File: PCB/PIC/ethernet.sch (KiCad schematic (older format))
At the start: 49 parts, among them P1 HR911105A, U1 LAN_8740, U2 SI502

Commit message: CIAA PIC footprints done
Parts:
- removed P1: HR911105A, symbol CONN_14
- added J5: RJ45-TRANSFO, symbol RJ45-TRANSFO
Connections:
- no-connect marks 5 -> 4
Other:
- note removed: "Verificar disponibilidad del conector Ethernet.\nAlternativa: Pulse J0011D01BNL."
- moved on the sheet: C1, C10, C11, C12, C13, C14, C15, C2, C3, C4, C5, C6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

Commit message: Correcciones al esquematico segun rev01
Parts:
- C1, C5, C9: symbol CP1 -> CP1-RESCUE-ciaa-pic
- C10, C11, C12, C13, C14, C15, C2, C3, C4, C6, C63, C7, C8: symbol C -> C-RESCUE-ciaa-pic
- J5: footprint (none) -> footprints:RJ45_TRANSFO
- R1, R10, R11, R113, R12, R13, R139, R14, R140, R15, R16, R17, R18, R19, R2, R20, R21, R3, R31, R4, R5, R6, R7, R8, R81, R9, R91, R92, R95: symbol R -> R-RESCUE-ciaa-pic
- U1: footprint ~ -> footprints:QFN32_Opendous
- U2: footprint ~ -> footprints:4SMD; symbol SI50X -> Si50X
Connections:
- net labels added: +Filter, CRS_DV, MDC, MDIO, RXCLK, RXD0, RXD1, RXD2, RXD3, RXER, RXN, RXP, TXD0, TXD1, TXEN, TXN, TXP, XTAL1, nRST
- wire segments 144 -> 153
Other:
- note added: "Señales TXP,TXN RXP,RXN \n100 ohm par diferencial\n"
- moved on the sheet: C1, C10, C11, C12, C13, C14, C15, C2, C3, C4, C5, C6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

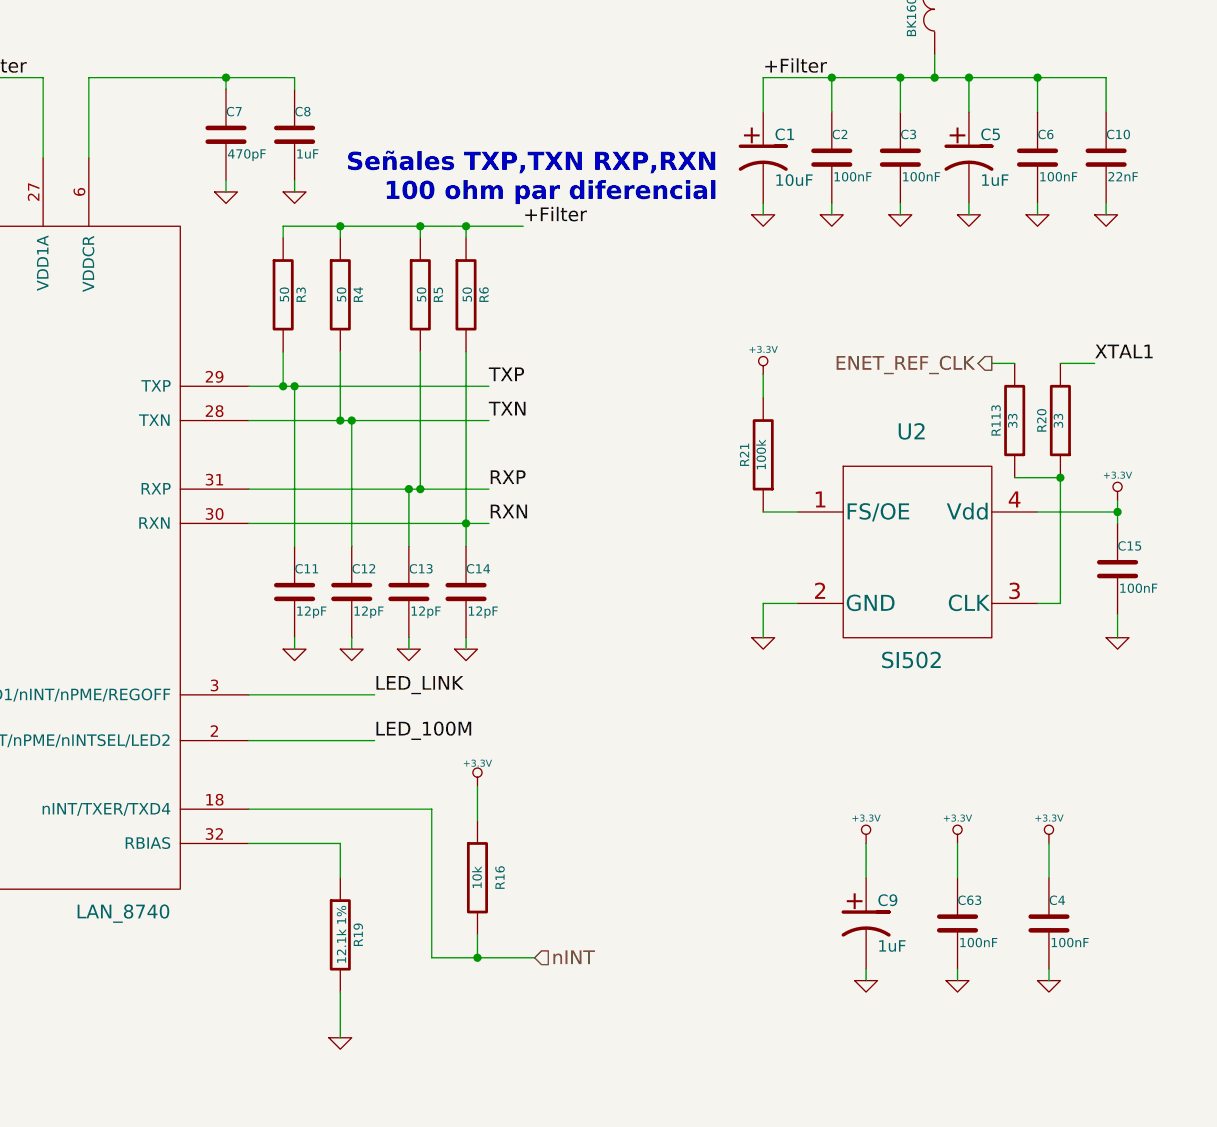
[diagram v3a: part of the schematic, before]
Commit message: elimino conector salida reles
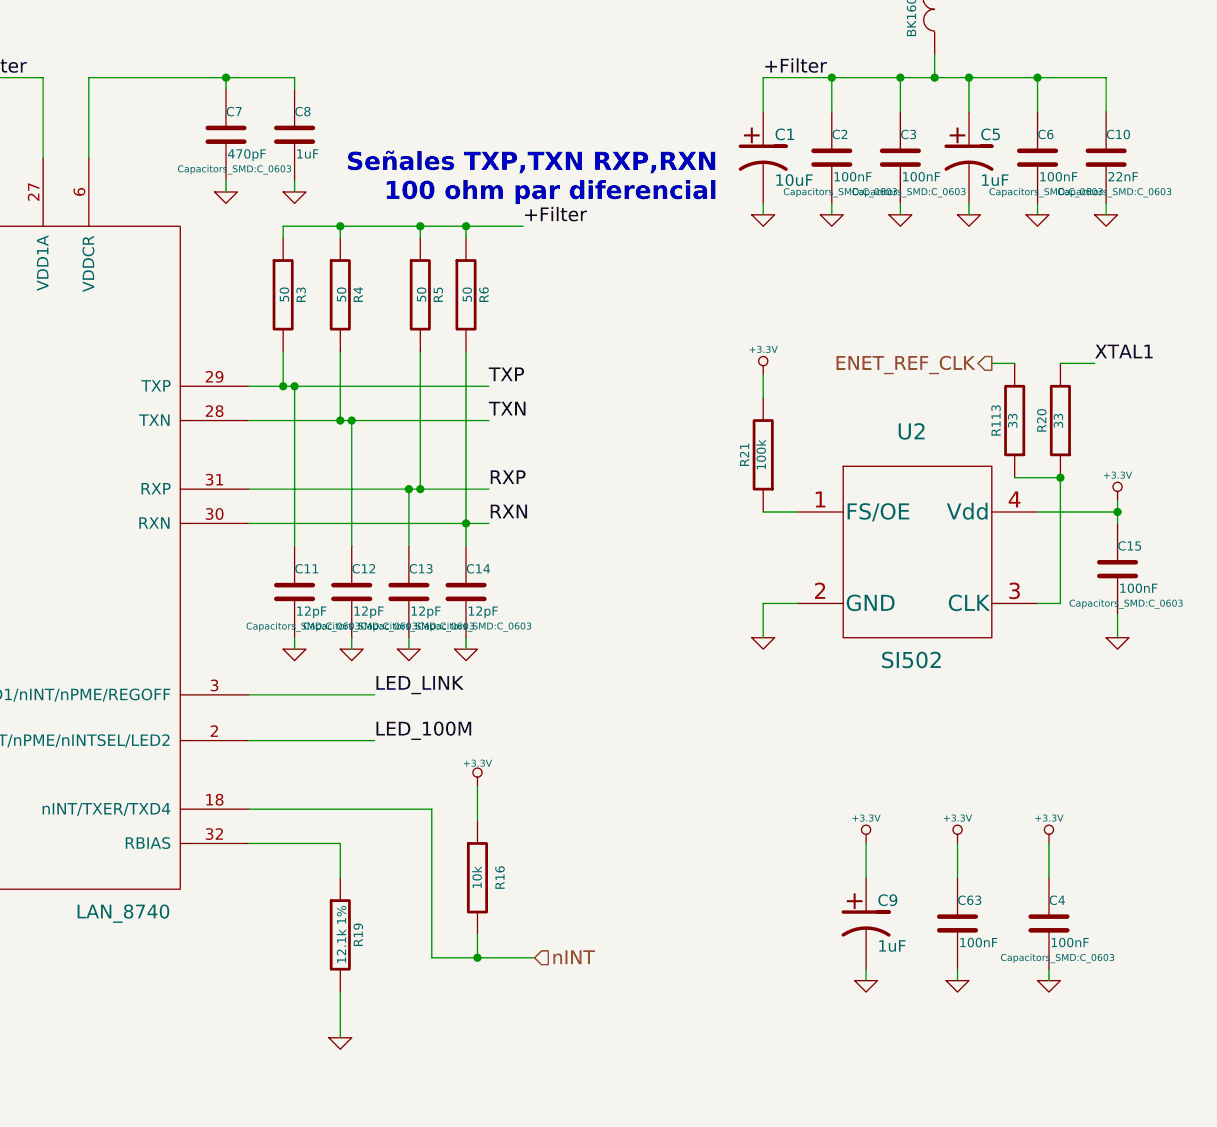
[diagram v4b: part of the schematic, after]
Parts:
- C1, C5, C8, C9, L1: footprint ~ -> (none)
- C10, C11, C12, C13, C14, C15, C2, C3, C4, C6, C63, C7: footprint ~ -> Capacitors_SMD:C_0603
- R1, R10, R11, R113, R12, R13, R139, R14, R140, R15, R16, R17, R18, R19, R2, R20, R21, R3, R31, R4, R5, R6, R7, R8, R81, R9, R91, R92, R95: footprint ~ -> Resistors_SMD:R_0603

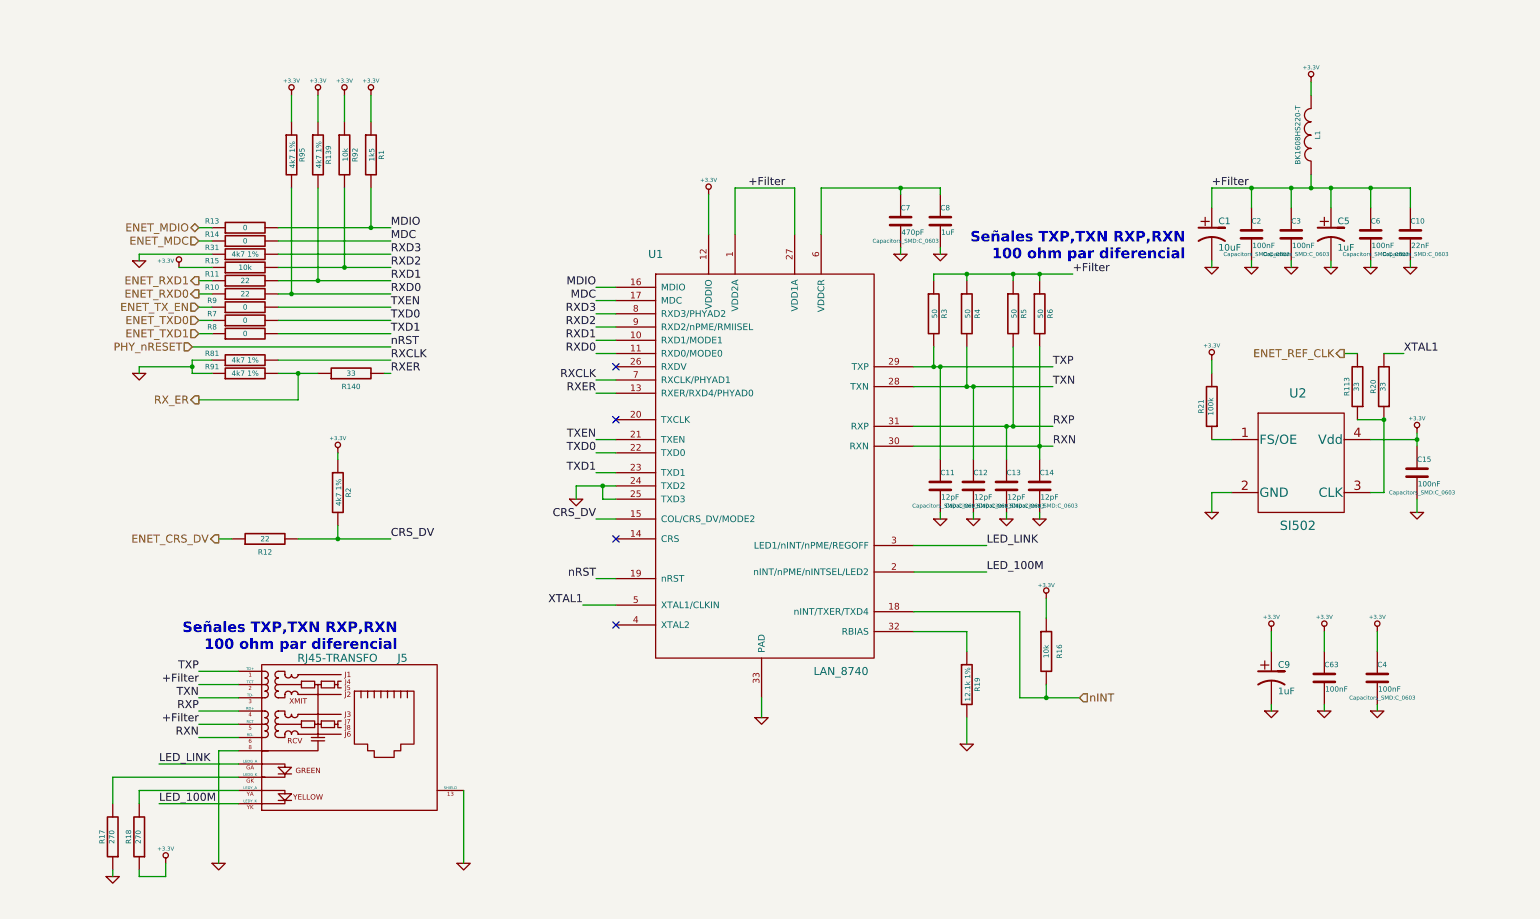
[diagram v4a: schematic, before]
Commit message: rev02 se completa campo num. de frabicante(#manf) CIAA-PIC
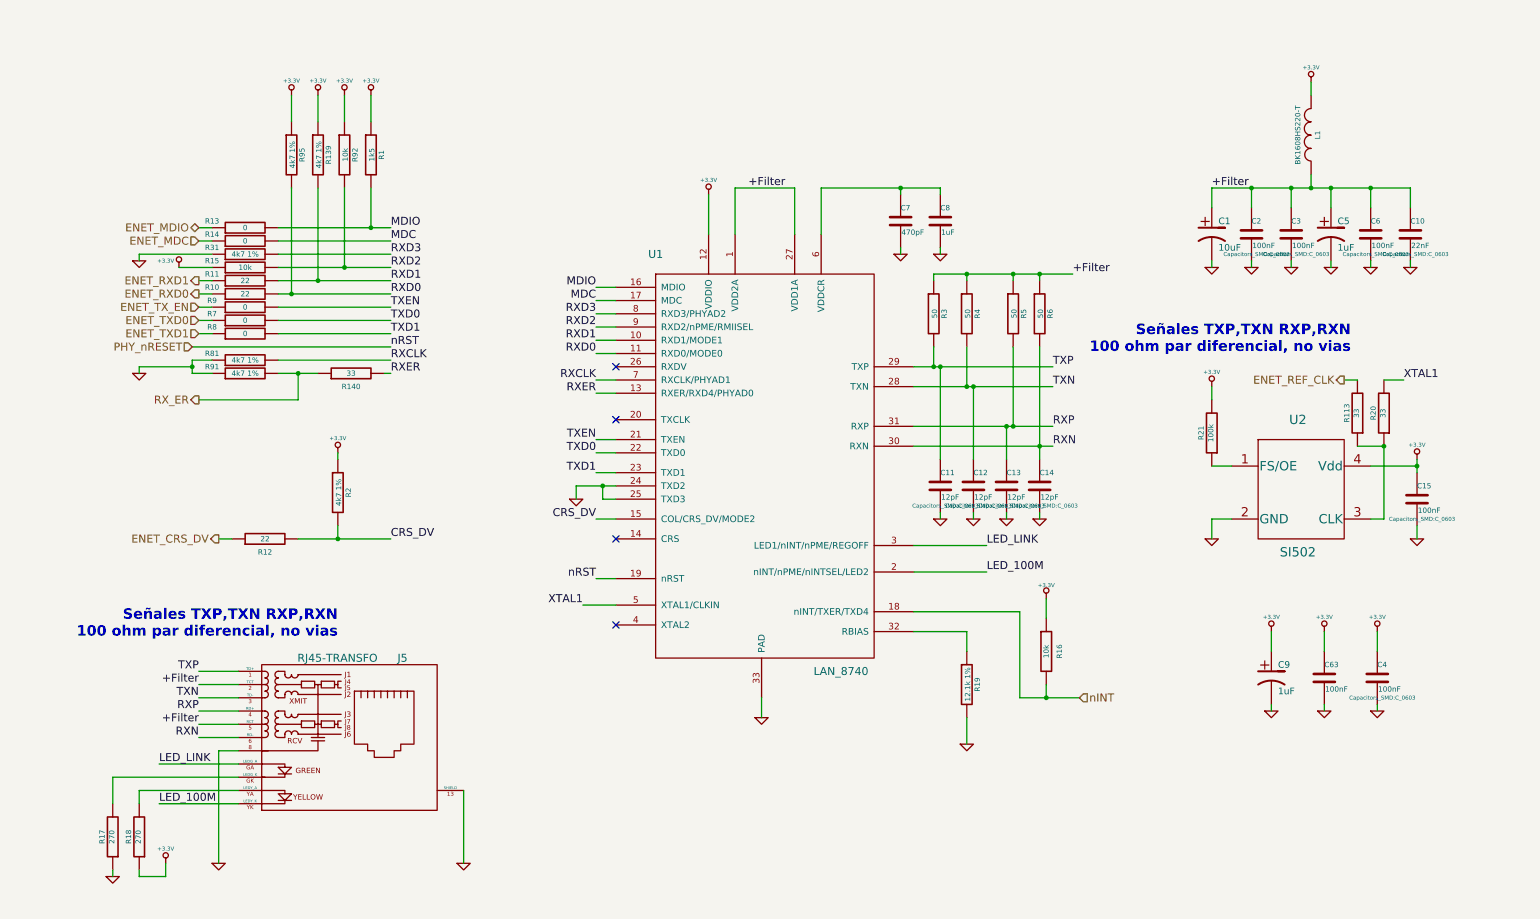
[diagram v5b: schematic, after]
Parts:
- R3, R4, R5, R6: #manf (none) -> RC0603FR-0749R9L
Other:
- note added: "Señales TXP,TXN RXP,RXN \n100 ohm par diferencial, no vias\n"
- note removed: "Señales TXP,TXN RXP,RXN \n100 ohm par diferencial\n"
- moved on the sheet: C15, R113, R20, R21, U2
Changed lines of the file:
@@
 F 0 "C7" H 6800 2250 40  0000 L CNN
 F 1 "470pF" H 6806 2065 40  0000 L CNN
-F 2 "Capacitors_SMD:C_0603" H 6838 2000 30  0000 C CNN
+F 2 "Capacitors_SMD:C_0603" H 6838 2000 30  0001 C CNN
 F 3 "~" H 6800 2150 60  0000 C CNN
 	1    6800 2150
@@
 F 2 "Resistors_SMD:R_0603" V 6980 2850 30  0001 C CNN
 F 3 "~" H 7050 2850 30  0000 C CNN
+F 4 "RC0603FR-0749R9L" V 7050 2850 60  0001 C CNN "#manf"
 	1    7050 2850
 	1    0    0    -1
@@
 F 2 "Resistors_SMD:R_0603" V 7230 2850 30  0001 C CNN
 F 3 "~" H 7300 2850 30  0000 C CNN
+F 4 "RC0603FR-0749R9L" V 7300 2850 60  0001 C CNN "#manf"
 	1    7300 2850
 	1    0    0    -1
@@
 F 2 "Resistors_SMD:R_0603" V 7580 2850 30  0001 C CNN
 F 3 "~" H 7650 2850 30  0000 C CNN
+F 4 "RC0603FR-0749R9L" V 7650 2850 60  0001 C CNN "#manf"
 	1    7650 2850
 	1    0    0    -1
@@
 F 2 "Resistors_SMD:R_0603" V 7780 2850 30  0001 C CNN
 F 3 "~" H 7850 2850 30  0000 C CNN
+F 4 "RC0603FR-0749R9L" V 7850 2850 60  0001 C CNN "#manf"
 	1    7850 2850
 	1    0    0    -1
@@
 L C-RESCUE-ciaa-pic C15
 U 1 1 529F82E9
-P 10700 4050
-F 0 "C15" H 10700 4150 40  0000 L CNN
-F 1 "100nF" H 10706 3965 40  0000 L CNN
-F 2 "Capacitors_SMD:C_0603" H 10738 3900 30  0000 C CNN
-F 3 "~" H 10700 4050 60  0000 C CNN
-	1    10700 4050
+P 10700 4250
+F 0 "C15" H 10700 4350 40  0000 L CNN
+F 1 "100nF" H 10706 4165 40  0000 L CNN
+F 2 "Capacitors_SMD:C_0603" H 10738 4100 30  0000 C CNN
+F 3 "~" H 10700 4250 60  0000 C CNN
+	1    10700 4250
 	1    0    0    -1
 $EndComp
@@
 L Si50X U2
 U 1 1 52BC24C2
-P 9800 4000
-F 0 "U2" H 9800 4550 70  0000 C CNN
-F 1 "SI502" H 9800 3550 70  0000 C CNN
-F 2 "footprints:4SMD" H 9850 3450 60  0001 C CNN
-F 3 "http://www.digikey.com/product-detail/en/silicon-labs/502AAA-ADAG/502AAA-ADAG-ND/4173092" H 8750 7300 60  0001 C CNN
-	1    9800 4000
+P 9800 4200
+F 0 "U2" H 9800 4750 70  0000 C CNN
+F 1 "SI502" H 9800 3750 70  0000 C CNN
+F 2 "footprints:4SMD" H 9850 3650 60  0001 C CNN
+F 3 "http://www.digikey.com/product-detail/en/silicon-labs/502AAA-ADAG/502AAA-ADAG-ND/4173092" H 8750 7500 60  0001 C CNN
+	1    9800 4200
 	1    0    0    -1
 $EndComp
@@
 L +3.3V-RESCUE-ciaa-pic #PWR018
 U 1 1 52BC26E1
-P 10700 3750
-F 0 "#PWR018" H 10700 3710 30  0001 C CNN
-F 1 "+3.3V" H 10700 3860 30  0000 C CNN
-F 2 "" H 10700 3750 60  0000 C CNN
-F 3 "" H 10700 3750 60  0000 C CNN
-	1    10700 3750
+P 10700 3950
+F 0 "#PWR018" H 10700 3910 30  0001 C CNN
+F 1 "+3.3V" H 10700 4060 30  0000 C CNN
+F 2 "" H 10700 3950 60  0000 C CNN
+F 3 "" H 10700 3950 60  0000 C CNN
+	1    10700 3950
 	1    0    0    -1
 $EndComp
@@
 L GND-RESCUE-ciaa-pic #PWR019
 U 1 1 52BC278C
-P 9150 4350
-F 0 "#PWR019" H 9150 4350 30  0001 C CNN
-F 1 "GND" H 9150 4280 30  0001 C CNN
-F 2 "" H 9150 4350 60  0000 C CNN
-F 3 "" H 9150 4350 60  0000 C CNN
-	1    9150 4350
+P 9150 4550
+F 0 "#PWR019" H 9150 4550 30  0001 C CNN
+F 1 "GND" H 9150 4480 30  0001 C CNN
+F 2 "" H 9150 4550 60  0000 C CNN
+F 3 "" H 9150 4550 60  0000 C CNN
+	1    9150 4550
 	1    0    0    -1
 $EndComp
@@
 L R-RESCUE-ciaa-pic R20
 U 1 1 52BC2833
-P 10450 3400
-F 0 "R20" V 10530 3400 40  0000 C CNN
-F 1 "33" V 10457 3401 40  0000 C CNN
-F 2 "Resistors_SMD:R_0603" V 10380 3400 30  0001 C CNN
-F 3 "~" H 10450 3400 30  0000 C CNN
-	1    10450 3400
+P 10450 3600
+F 0 "R20" V 10530 3600 40  0000 C CNN
+F 1 "33" V 10457 3601 40  0000 C CNN
+F 2 "Resistors_SMD:R_0603" V 10380 3600 30  0001 C CNN
+F 3 "~" H 10450 3600 30  0000 C CNN
+	1    10450 3600
 	-1   0    0    1
 $EndComp
@@
 L GND-RESCUE-ciaa-pic #PWR022
 U 1 1 52BC2B5C
-P 10700 4350
-F 0 "#PWR022" H 10700 4350 30  0001 C CNN
-F 1 "GND" H 10700 4280 30  0001 C CNN
-F 2 "" H 10700 4350 60  0000 C CNN
-F 3 "" H 10700 4350 60  0000 C CNN
-	1    10700 4350
+P 10700 4550
+F 0 "#PWR022" H 10700 4550 30  0001 C CNN
+F 1 "GND" H 10700 4480 30  0001 C CNN
+F 2 "" H 10700 4550 60  0000 C CNN
+F 3 "" H 10700 4550 60  0000 C CNN
+	1    10700 4550
 	1    0    0    -1
 $EndComp
@@
 L R-RESCUE-ciaa-pic R21
 U 1 1 52BC2C7C
-P 9150 3550
-F 0 "R21" V 9230 3550 40  0000 C CNN
-F 1 "100k" V 9157 3551 40  0000 C CNN
-F 2 "Resistors_SMD:R_0603" V 9080 3550 30  0001 C CNN
-F 3 "~" H 9150 3550 30  0000 C CNN
-	1    9150 3550
+P 9150 3750
+F 0 "R21" V 9230 3750 40  0000 C CNN
+F 1 "100k" V 9157 3751 40  0000 C CNN
+F 2 "Resistors_SMD:R_0603" V 9080 3750 30  0001 C CNN
+F 3 "~" H 9150 3750 30  0000 C CNN
+	1    9150 3750
 	-1   0    0    1
 $EndComp
@@
 L +3.3V-RESCUE-ciaa-pic #PWR023
 U 1 1 52BC2DB0
-P 9150 3200
-F 0 "#PWR023" H 9150 3160 30  0001 C CNN
-F 1 "+3.3V" H 9150 3310 30  0000 C CNN
-F 2 "" H 9150 3200 60  0000 C CNN
-F 3 "" H 9150 3200 60  0000 C CNN
-	1    9150 3200
-	1    0    0    -1
-$EndComp
-Text HLabel 10150 3150 0    60   Output ~ 0
+P 9150 3400
+F 0 "#PWR023" H 9150 3360 30  0001 C CNN
+F 1 "+3.3V" H 9150 3510 30  0000 C CNN
+F 2 "" H 9150 3400 60  0000 C CNN
+F 3 "" H 9150 3400 60  0000 C CNN
+	1    9150 3400
+	1    0    0    -1
+$EndComp
+Text HLabel 10150 3350 0    60   Output ~ 0
 ENET_REF_CLK
 $Comp
@@
 	10400 5250 10400 5400
 Wire Wire Line
-	10350 3800 10700 3800
-Wire Wire Line
-	10700 3750 10700 3850
-Connection ~ 10700 3800
-Wire Wire Line
-	9300 4200 9150 4200
-Wire Wire Line
-	9150 4200 9150 4350
-Wire Wire Line
-	10450 4200 10350 4200
-Wire Wire Line
-	10450 3650 10450 4200
+	10350 4000 10700 4000
+Wire Wire Line
+	10700 3950 10700 4050
+Connection ~ 10700 4000
+Wire Wire Line
+	9300 4400 9150 4400
+Wire Wire Line
+	9150 4400 9150 4550
+Wire Wire Line
+	10450 4400 10350 4400
+Wire Wire Line
+	10450 3850 10450 4400
 Wire Wire Line
 	1350 2500 1600 2500
 Wire Wire Line
-	10700 4250 10700 4350
-Wire Wire Line
-	9150 3800 9300 3800
-Wire Wire Line
-	9150 3300 9150 3200
-Wire Wire Line
-	10250 3150 10150 3150
+	10700 4450 10700 4550
+Wire Wire Line
+	9150 4000 9300 4000
+Wire Wire Line
+	9150 3500 9150 3400
+Wire Wire Line
+	10250 3350 10150 3350
 Wire Wire Line
 	1050 7100 1250 7100
@@
 L R-RESCUE-ciaa-pic R113
 U 1 1 538E2D29
-P 10250 3400
-F 0 "R113" V 10330 3400 40  0000 C CNN
-F 1 "33" V 10257 3401 40  0000 C CNN
-F 2 "Resistors_SMD:R_0603" V 10180 3400 30  0001 C CNN
-F 3 "~" H 10250 3400 30  0000 C CNN
-	1    10250 3400
+P 10250 3600
+F 0 "R113" V 10330 3600 40  0000 C CNN
+F 1 "33" V 10257 3601 40  0000 C CNN
+F 2 "Resistors_SMD:R_0603" V 10180 3600 30  0001 C CNN
+F 3 "~" H 10250 3600 30  0000 C CNN
+	1    10250 3600
 	-1   0    0    1
 $EndComp
 Wire Wire Line
-	10250 3650 10450 3650
-Connection ~ 10450 3650
+	10250 3850 10450 3850
+Connection ~ 10450 3850
 Wire Wire Line
 	2100 3300 2400 3300
@@
 RXN
 Wire Wire Line
-	10450 3150 10600 3150
+	10450 3350 10600 3350
 Wire Wire Line
 	4650 5050 4400 5050
-Text Label 10600 3150 0    60   ~ 0
+Text Label 10600 3350 0    60   ~ 0
 XTAL1
 Text Label 4400 5050 2    60   ~ 0
@@
 Wire Wire Line
 	1250 7100 1250 7000
-Text Notes 8950 2450 2    79   ~ 16
-Señales TXP,TXN RXP,RXN \n100 ohm par diferencial\n
-Text Notes 3000 5400 2    79   ~ 16
-Señales TXP,TXN RXP,RXN \n100 ohm par diferencial\n
+Text Notes 10200 3150 2    79   ~ 16
+Señales TXP,TXN RXP,RXN \n100 ohm par diferencial, no vias\n
+Text Notes 2550 5300 2    79   ~ 16
+Señales TXP,TXN RXP,RXN \n100 ohm par diferencial, no vias\n
 $EndSCHEMATC
